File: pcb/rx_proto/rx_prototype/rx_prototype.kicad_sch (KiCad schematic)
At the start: 1 part, among them U1 nRF52840

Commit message: Save progress of prototype board
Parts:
- added C1, C8: 10nF, symbol Device:C_Small
- added C10, C12, C3, C6: 330pF, symbol Device:C_Small
- added C11, C13, C4, C5: 0.47uF, symbol Device:C_Small
- added C14, C7: 1nF, symbol Device:C_Small
- added C2, C9: 47nF, symbol Device:C_Small
- added L1, L4: 2mH, symbol Device:L
- added L3: L, symbol Device:L
- added R1, R2: 10K, symbol Device:R_US
- added R10, R11, R4, R5, R6, R9: 6.8K, symbol Device:R_US
- added R12, R7: 2.2K, symbol Device:R_US
- added R3, R8: 560, symbol Device:R_US
- added U2: MPU-6500, symbol library:MPU-6500
- added U3: QMC5883P, symbol library:QMC5883P
- added U4, U5: MCP6004, symbol Amplifier_Operational:MCP6004
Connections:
- net ADC_1: now reaches U1.A10 (AIN5/P0.29)
- net ADC_0: now reaches U1.A12 (AIN0/P0.02)
- net +3.3V: now reaches U1.A22 (VDD), U1.AD14 (VDD), U1.AD23 (VDD), U1.B1 (VDD), U1.W1 (VDD)
- net +3.3V: now also R2.1, U2.13 (VDD), U3.2 (VDD), U4.4 (V+), U5.4 (V+)
- net ADC_2: now reaches U1.A8 (AIN7/P0.31)
- net SDA: now reaches U1.AD12 (P0.17)
- net SDA: now also U2.24 (SDA/SDI), U3.16 (SDA)
- net SCK: now reaches U1.AD16 (P0.20)
- net SCK: now also U2.23 (SCL/SCLK), U3.1 (SCK)
- net GND: now reaches U1.B7 (VSS), U1.EP (VSS)
- net GND: now also R1.2, U2.18 (GND), U3.9 (GND), U4.11 (V-), U5.11 (V-)
- new net: C5.2, C6.2, R6.1, U5.1
- new net: C12.2, C13.2, R11.1, U5.7
- new net: C12.1, R10.1, R11.2, U5.6 (-)
- new net: C2.1, R3.2
- new net: C10.1, R8.1, R9.2, U4.6 (-)
- new net: C9.1, R8.2
- new net: C11.2, R10.2
- new net: C6.1, R5.1, R6.2, U5.2 (-)
- new net: C3.1, R3.1, R4.2, U4.2 (-)
- new net: C4.2, R5.2
- new net: C1.1, L1.1, U4.3 (+)
- new net: C8.1, L4.1, U4.5 (+)
- new net V_BIAS: C1.2, C11.1, C14.1, C2.2, C4.1, C7.1, C8.2, C9.2, L1.2, L4.2, R1.1, R12.2, R2.2, R7.2
- new net V_OUT1: C3.2, R4.1, U4.1, U5.3 (+)
- new net V_OUT2: C5.1, C7.2, R7.1
- new net V_OUT3: C10.2, R9.1, U4.7, U5.5 (+)
- new net V_OUT4: C13.1, C14.2, R12.1
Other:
- moved on the sheet: U1

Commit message: Back up prototype
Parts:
- removed L3: L, symbol Device:L
- added C15: 10nF, symbol Device:C_Small
- added C16: 47nF, symbol Device:C_Small
- added C17, C19: 330pF, symbol Device:C_Small
- added C18: 0.47uF, symbol Device:C_Small
- added C20: 100nF, symbol Device:C_Small
- added C21: 1nF, symbol Device:C_Small
- added C22: 2.2nf, symbol Device:C_Small
- added C23, C24: 2.2nF, symbol Device:C_Small
- added C25, C26, C27, C28: 0.1uF, symbol Device:C_Small
- added L4: 2mH, symbol Device:L
- added R13, R15: 750, symbol Device:R_US
- added R14, R16: 6.8K, symbol Device:R_US
- added R17: 2.2K, symbol Device:R_US
- added U6: 74HC4051, symbol 74xx:74HC4051
- C1: value 10nF -> 33nF
- C13, C5: value 0.47uF -> 100nF
- L1: value 2mH -> 0.7mH
- R10, R5: value 6.8K -> 750
- R3, R8: value 560 -> 750
- renumbered L4 to L3
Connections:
- net +3.3V: now also C26.2, C27.2, U6.16 (VCC); no longer U4.4 (V+), U5.4 (V+)
- net GND: now also C25.1, C28.1, U6.8 (GND); no longer U4.11 (V-), U5.11 (V-)
- net V_BIAS: now also U5.8, U5.9 (-), C15.2, C16.2, C18.1, C21.1, C22.2, C23.2, C24.2, L4.2, R17.2; no longer R1.1, R2.2
- net V_OUT5: now reaches U4.12 (+)
- net V_OUT5: now also U4.8, C17.2, R14.1
- net at U4.13 (-): now also C19.1, R15.1, R16.2
- net at U5.10 (+): now also R1.1, R2.2
- net at C1.1, L1.1, U4.3 (+): now also C22.1
- net at C8.1, L3.1, U4.5 (+): now also C23.1
- net at U4.10 (+): now also C15.1, C24.1, L4.1
- net at U4.9 (-): now also C17.1, R13.1, R14.2
- new net: C18.2, R15.2
- new net: C28.2, U4.11 (V-)
- new net: C19.2, C20.2, R16.1
- new net: C16.1, R13.2
- new net: C25.2, U5.11 (V-)
- new net: C26.1, U5.4 (V+)
- new net: C27.1, U4.4 (V+)
- new net V_OUT6: C20.1, C21.2, R17.1
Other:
- note added: "R3 should be 51, check research paper"
- note added: "R5 should be 51, but MCP6004 limited to 1MHZ replace when using better op amp"
- note added: "analog digital front end"
- note added: "stage 1 uses negative feedback to amplify 32khz signal using differentiator circuit to amplifer oscilations"
- note added: "unity gain amplifer used to isolate vbias"
- moved on the sheet: C1, C10, C11, C12, C13, C14, C2, C3, C4, C5, C6, C7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

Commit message: Another prototype backup
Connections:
- net ADC_0: now also U5.13 (-), U5.14
- net GND: now also U6.2 (A6), U6.4 (A7), U6.6 (~{E}), U6.7 (VEE)
- net V_OUT1: now also U6.13 (A0)
- net V_OUT2: now also U6.14 (A1)
- net V_OUT3: now also U6.15 (A2)
- net V_OUT4: now also U6.12 (A3)
- net V_OUT5: now also U6.1 (A4)
- net V_OUT6: now also U6.5 (A5)
- net ADC_BUFFER: now reaches U5.12 (+)
- net ADC_BUFFER: now also U6.3 (A)
- net SELECT_1: now reaches U6.10 (S1)
- net SELECT_1: now also U1.U24 (P1.04)
- net SELECT_0: now reaches U6.11 (S0)
- net SELECT_0: now also U1.R24 (P1.06)
- net SELECT_2: now reaches U6.9 (S2)
- net SELECT_2: now also U1.Y23 (P1.01)
- net ADC_1: no longer names the net of U1.A10 (AIN5/P0.29)
- net ADC_2: no longer names the net of U1.A8 (AIN7/P0.31)
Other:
- moved on the sheet: C25, C26, C27, C28, U4E, U5D, U5E, U6

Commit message: Update wiring
capcitors were in parallel would cause DC blocking
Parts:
- removed C25, C28: 0.1uF, symbol Device:C_Small
- added C29: 0.1uF, symbol Device:C_Small
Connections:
- net +3.3V: now also C27.1, U4.4 (V+), U5.4 (V+); no longer C27.2
- net GND: now also C26.1, C27.2, U4.11 (V-), U5.11 (V-), C29.1
- net at R1.1, R2.2, U5.10 (+): now also C29.2
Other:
- moved on the sheet: C26, C27

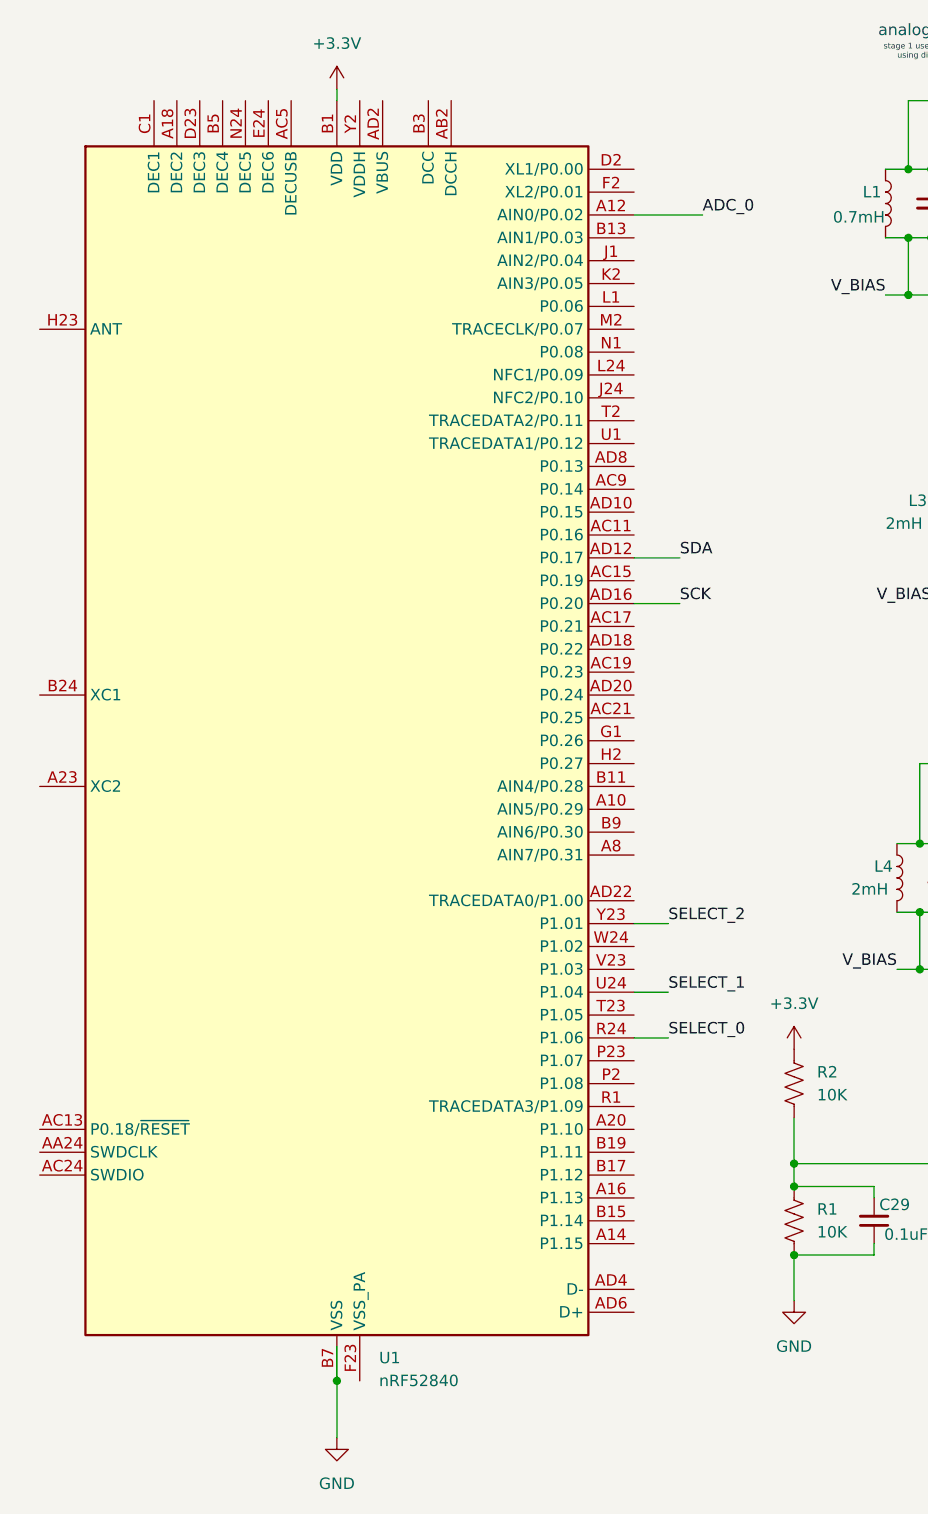
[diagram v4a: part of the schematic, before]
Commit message: Update prototype to include footprints for perfboard layout
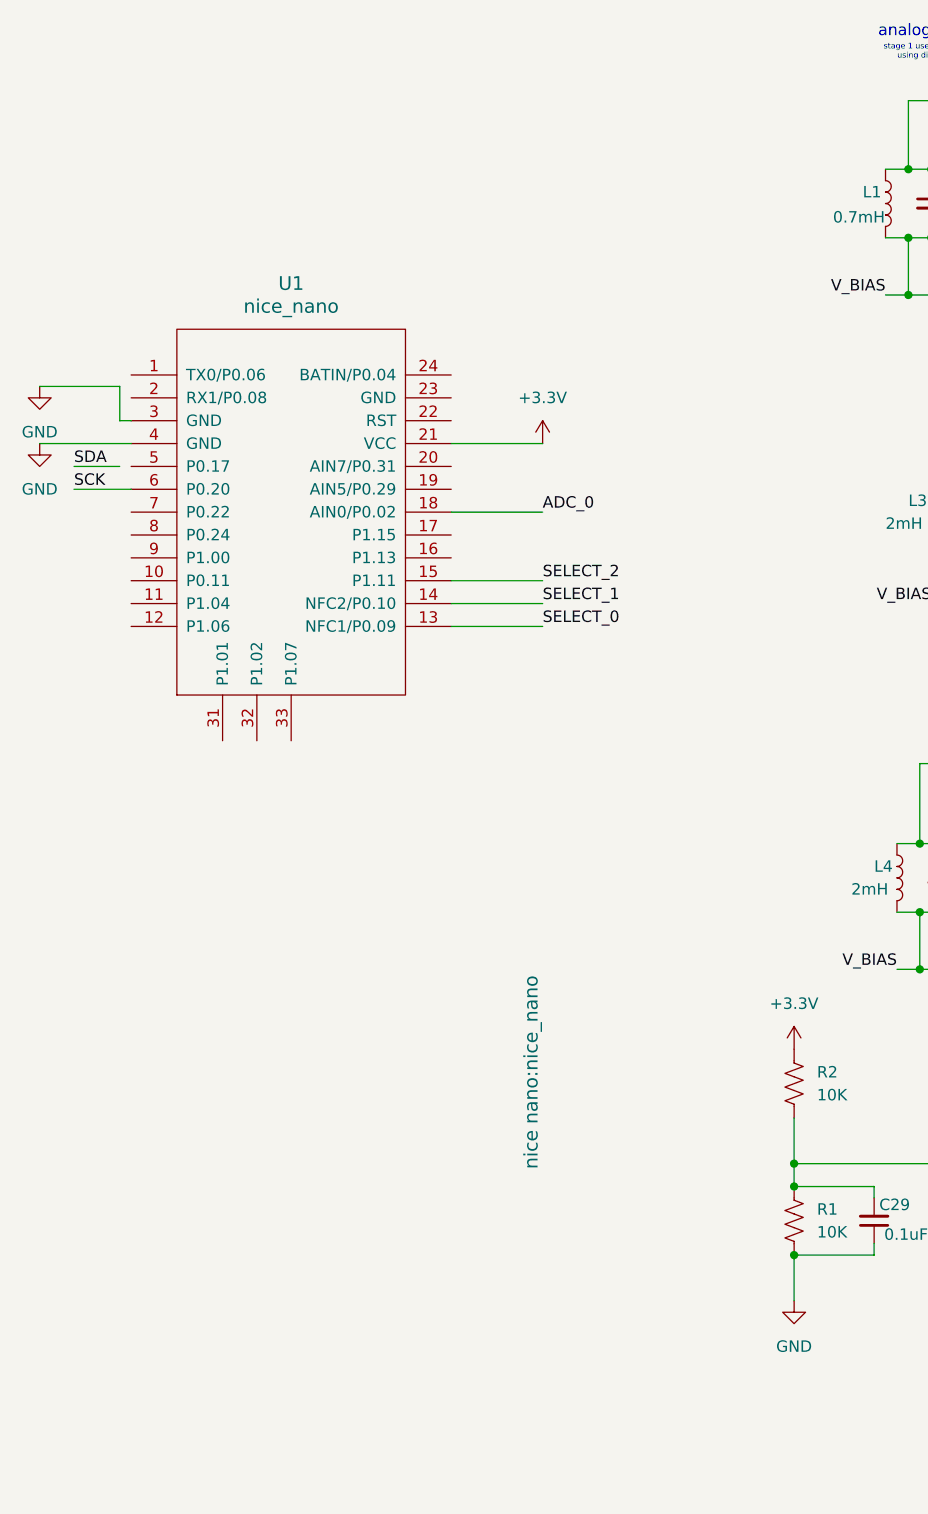
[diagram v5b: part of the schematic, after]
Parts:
- removed U1: nRF52840, Package_DFN_QFN:Nordic_AQFN-73-1EP_7x7mm_P0.5mm, symbol MCU_Nordic:nRF52840
- added U1: nice_nano, nice nano:nice_nano, symbol nice_nano:nice_nano
- U4, U5: footprint (none) -> Library:MCP6004
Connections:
- net +3.3V: now also U1.21 (VCC)
- net ADC_0: now also U1.18 (AIN0/P0.02)
- net GND: now also U1.3 (GND), U1.4 (GND)
- net SCK: now also U1.6 (P0.20)
- net SELECT_0: now also U1.13 (NFC1/P0.09)
- net SELECT_1: now also U1.14 (NFC2/P0.10)
- net SELECT_2: now also U1.15 (P1.11)

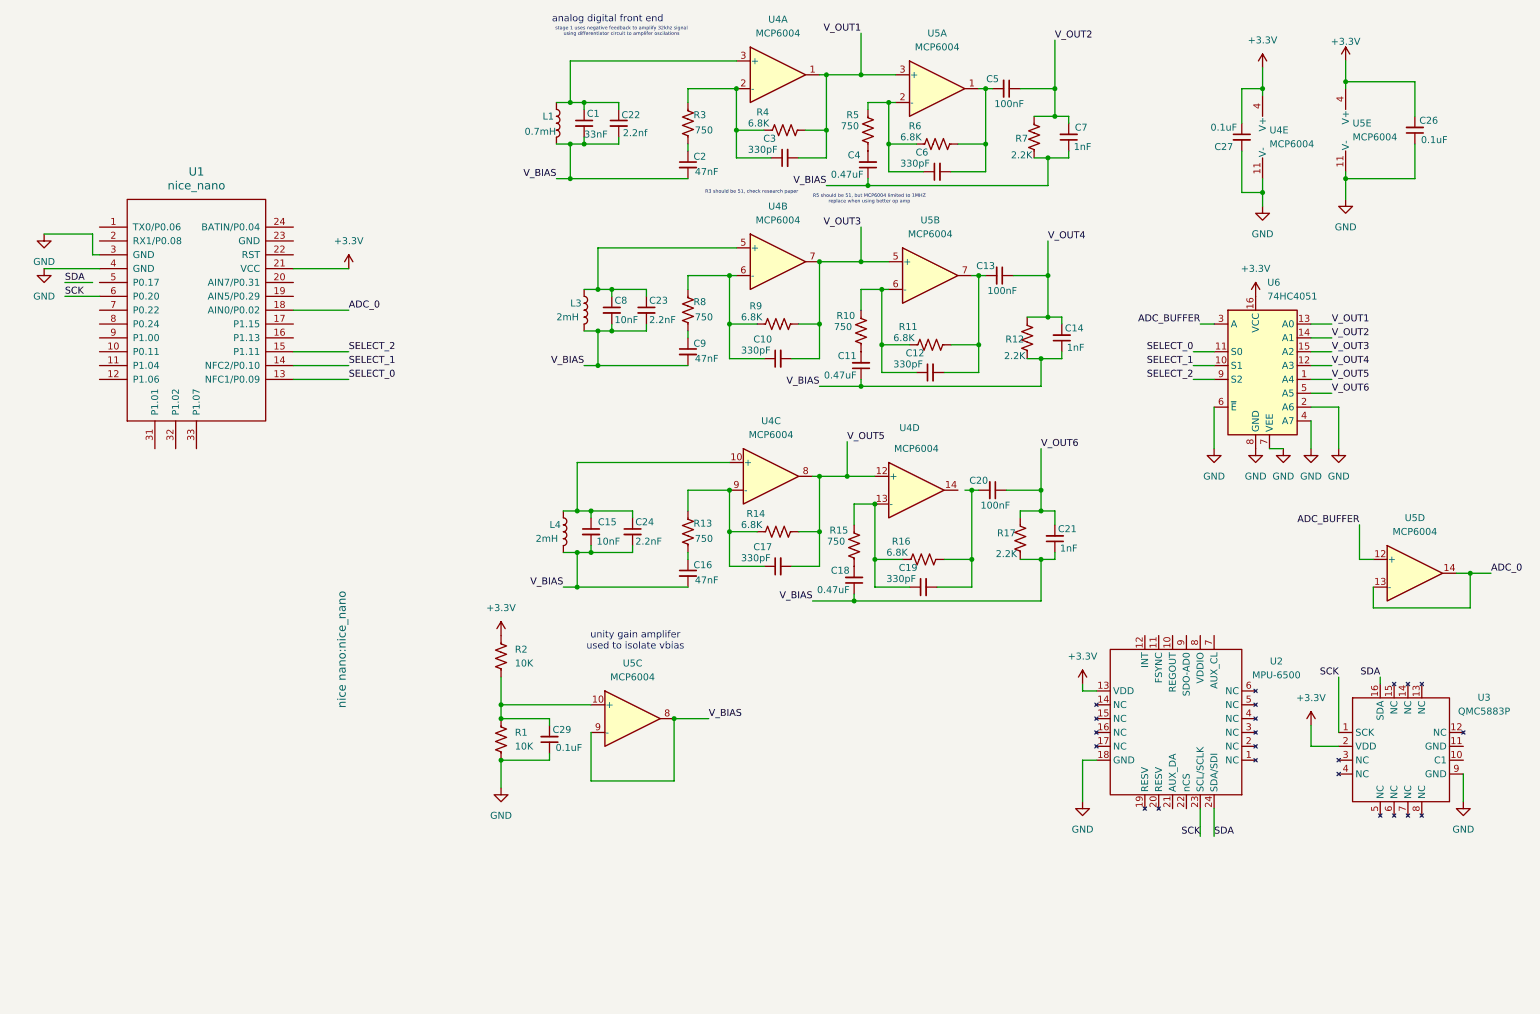
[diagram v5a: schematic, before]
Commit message: Update perfboard layout
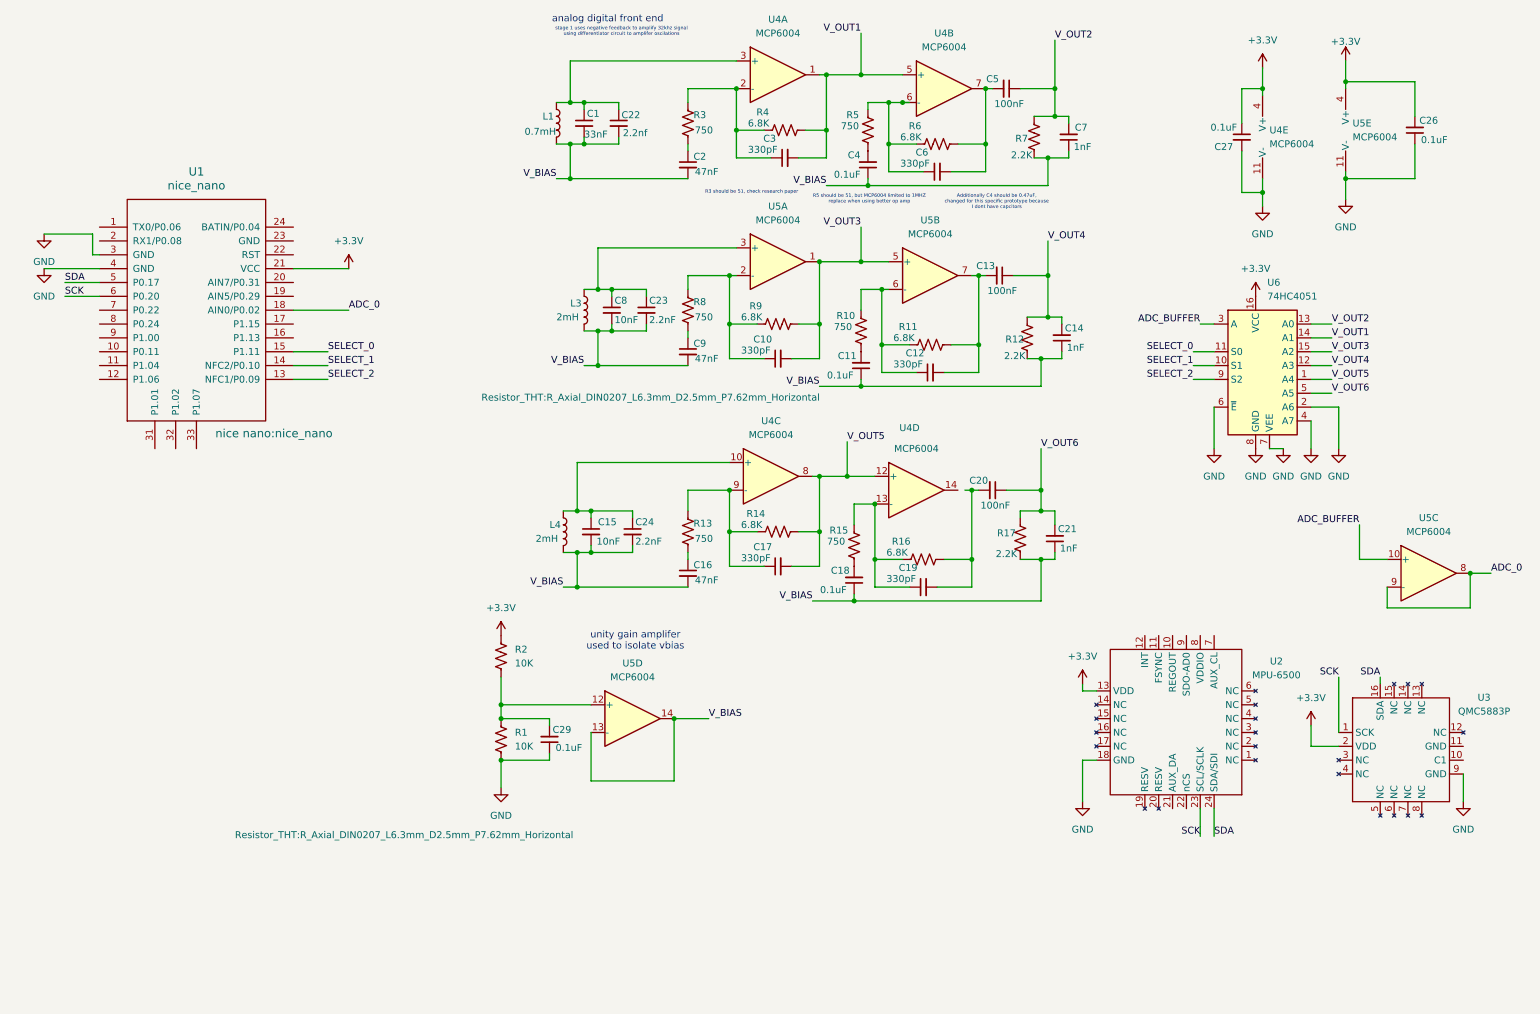
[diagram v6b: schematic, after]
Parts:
- C1, C10, C12, C13, C14, C15, C16, C17, C19, C2, C20, C21, C22, C23, C24, C26, C27, C29, C3, C5, C6, C7, C8, C9: footprint (none) -> Capacitor_THT:C_Disc_D5.0mm_W2.5mm_P5.00mm
- C11, C18, C4: value 0.47uF -> 0.1uF; footprint (none) -> Capacitor_THT:C_Disc_D5.0mm_W2.5mm_P5.00mm
- R1, R10, R11, R12, R13, R14, R15, R16, R17, R2, R3, R4, R5, R6, R7, R8, R9: footprint (none) -> Resistor_THT:R_Axial_DIN0207_L6.3mm_D2.5mm_P7.62mm_Horizontal
- U2: footprint (none) -> Library:MPU-6500
- U3: footprint (none) -> Library:QMC5883P
- U6: footprint (none) -> Library:74HC4051
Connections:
- net ADC_0: now also U5.8, U5.9 (-); no longer U5.13 (-), U5.14
- net ADC_BUFFER: now also U5.10 (+); no longer U5.12 (+)
- net SDA: now also U1.5 (P0.17)
- net SELECT_0: now also U1.15 (P1.11); no longer U1.13 (NFC1/P0.09)
- net SELECT_2: now also U1.13 (NFC1/P0.09); no longer U1.15 (P1.11)
- net V_BIAS: now also U5.13 (-), U5.14; no longer U5.8, U5.9 (-)
- net V_OUT1: now also U4.5 (+), U6.14 (A1); no longer U5.3 (+), U6.13 (A0)
- net V_OUT2: now also U6.13 (A0); no longer U6.14 (A1)
- net V_OUT3: now also U5.1; no longer U4.7
- net at C5.2, C6.2, R6.1: now also U4.7; no longer U5.1
- net at C29.2, R1.1, R2.2: now also U5.12 (+); no longer U5.10 (+)
- net at C10.1, R8.1, R9.2: now also U5.2 (-); no longer U4.6 (-)
- net at C6.1, R5.1, R6.2: now also U4.6 (-); no longer U5.2 (-)
- net at C23.1, C8.1, L3.1: now also U5.3 (+); no longer U4.5 (+)
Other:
- note added: "Additionally C4 should be 0.47uF, changed for this specific prototype because I dont have capcitors"
- moved on the sheet: U4B, U5A, U5C, U5D

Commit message: Update perf layout
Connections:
- net V_OUT1: now also U6.13 (A0); no longer U6.14 (A1)
- net V_OUT2: now also U6.14 (A1); no longer U6.13 (A0)
- net V_OUT3: now also C17.2, R14.1, U4.10 (+), U4.14; no longer C10.2, R9.1, U5.1, U5.5 (+)
- net V_OUT4: now also C20.1, C21.2, R17.1; no longer C13.1, C14.2, R12.1
- net V_OUT5: now also C10.2, R9.1, U5.1, U5.5 (+); no longer C17.2, R14.1, U4.12 (+), U4.8
- net V_OUT6: now also C13.1, C14.2, R12.1; no longer C20.1, C21.2, R17.1
- net at C19.1, R15.1, R16.2: now also U4.9 (-); no longer U4.13 (-)
- net at C15.1, C24.1, L4.1: now also U4.12 (+); no longer U4.10 (+)
- net at C17.1, R13.1, R14.2: now also U4.13 (-); no longer U4.9 (-)
- net at C19.2, C20.2, R16.1: now also U4.8
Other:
- moved on the sheet: C10, C11, C12, C13, C14, C15, C16, C17, C18, C19, C20, C21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

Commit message: Update perf
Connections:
- net V_OUT1: now also C17.2, R14.1, U4.10 (+), U4.14, U6.14 (A1); no longer C3.2, R4.1, U4.1, U4.5 (+), U6.13 (A0)
- net V_OUT2: now also C20.1, C21.2, R17.1, U6.13 (A0); no longer C5.1, C7.2, R7.1, U6.14 (A1)
- net V_OUT3: now also C3.2, R4.1, U4.1, U4.5 (+), U6.12 (A3); no longer C17.2, R14.1, U4.10 (+), U4.14, U6.15 (A2)
- net V_OUT4: now also C5.1, C7.2, R7.1, U6.15 (A2); no longer C20.1, C21.2, R17.1, U6.12 (A3)
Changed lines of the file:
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@@
 		)
 	)
-	(label "V_OUT1"
+	(label "V_OUT3"
 		(at 165.1 17.78 180)
 		(effects
@@
 		)
 	)
-	(label "V_OUT2"
+	(label "V_OUT1"
 		(at 251.46 73.66 0)
 		(effects
@@
 		)
 	)
-	(label "V_OUT1"
+	(label "V_OUT2"
 		(at 251.46 71.12 0)
 		(effects
@@
 		)
 	)
-	(label "V_OUT2"
+	(label "V_OUT4"
 		(at 200.66 19.05 0)
 		(effects
@@
 		)
 	)
-	(label "V_OUT4"
+	(label "V_OUT3"
 		(at 251.46 78.74 0)
 		(effects
@@
 		)
 	)
-	(label "V_OUT3"
+	(label "V_OUT4"
 		(at 251.46 76.2 0)
 		(effects
@@
 		)
 	)
-	(label "V_OUT4"
+	(label "V_OUT2"
 		(at 191.77 59.69 0)
 		(effects
@@
 		)
 	)
-	(label "V_OUT3"
+	(label "V_OUT1"
 		(at 156.21 58.42 0)
 		(effects
